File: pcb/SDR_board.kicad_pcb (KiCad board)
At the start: 4 copper layers, 100 x 100 mm, 469 parts, among them J1 USB_B_Mini, J201 Molex 73251-1150 SMA, J301 Molex 73251-1150 SMA, J401 Molex 73251-1150 SMA, J501 Molex 73251-1150 SMA, SW1 SW_Push, U1 AMS1117-3.3, U2 NB3L553, U201 BGA2803, U202 MSi001-Q40, U203 MAX19777AZA+, U204 ADS7883, U205 LMV712-N, U206 MAX19777AZA+, U207 ADS7883, U3 CY7C68013A-56PVX, U301 BGA2803, U302 MSi001-Q40, U303 MAX19777AZA+, U304 ADS7883, U305 LMV712-N, U306 MAX19777AZA+, U307 ADS7883, U401 BGA2803, U402 MSi001-Q40, U403 MAX19777AZA+, U404 ADS7883, U405 LMV712-N, U406 MAX19777AZA+, U407 ADS7883, U5 24LC128, U501 BGA2803, U502 MSi001-Q40, U503 MAX19777AZA+, U504 ADS7883, U505 LMV712-N, U506 MAX19777AZA+, U507 ADS7883, U6 MCP1825S, X1 XO32, X2 XO32

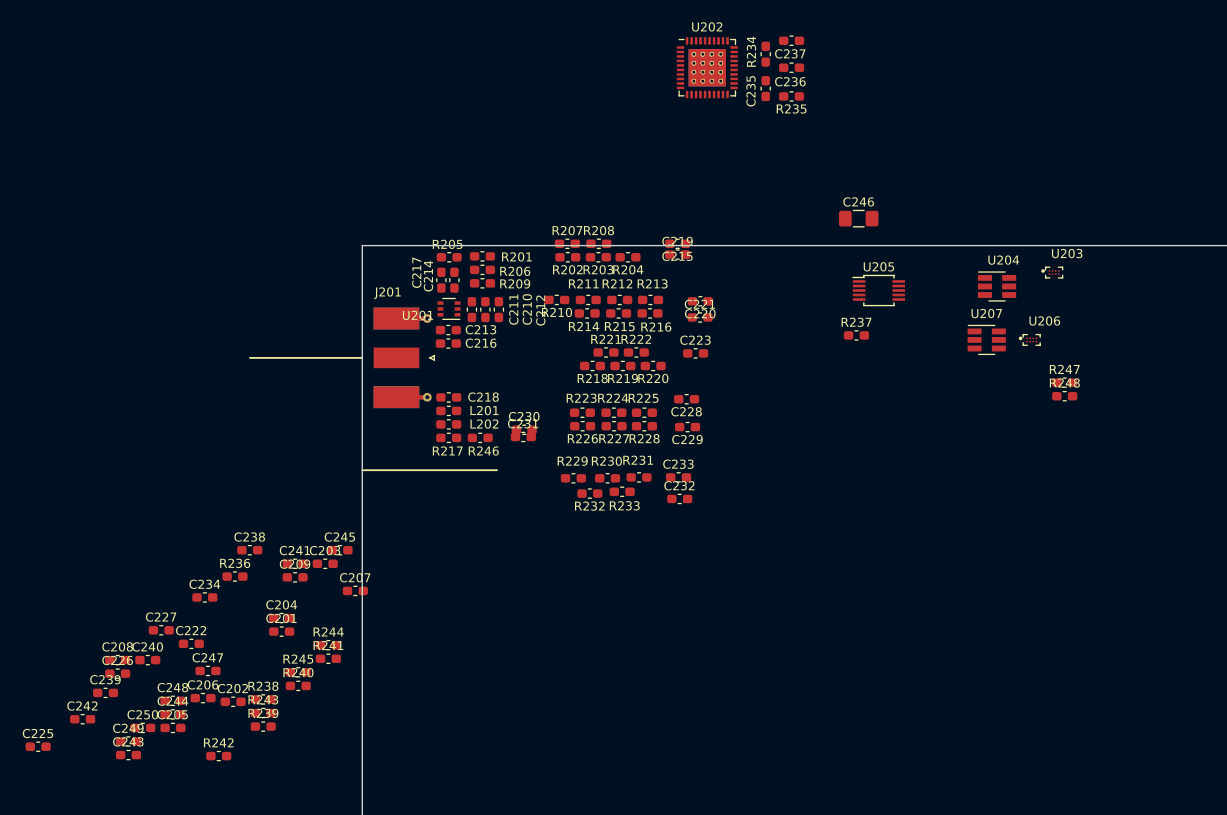
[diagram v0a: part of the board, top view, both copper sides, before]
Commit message: more component layout
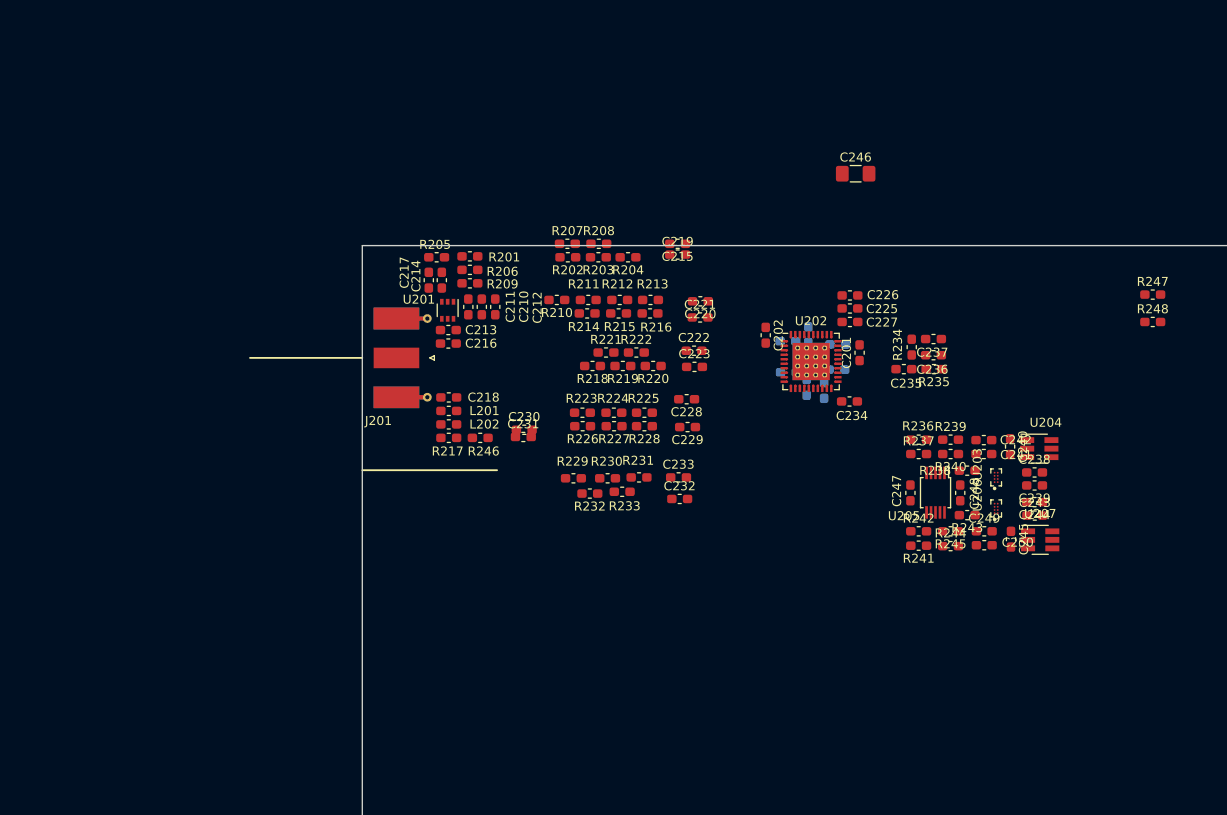
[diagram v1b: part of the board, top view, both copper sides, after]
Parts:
- C203, C204, C205, C206, C207, C208, C209: moved to B.Cu
- moved C239 105.9 mm to (99.8, 46.7), turned to 180 degrees
- moved C242 105.0 mm to (94.2, 41.6)
- moved C243 104.3 mm to (99.8, 50.0)
- moved C225 102.7 mm to (79.3, 27.0), turned to 180 degrees
- moved C240 98.9 mm to (97.1, 42.4), turned to 270 degrees
- moved C244 98.8 mm to (99.8, 48.5), turned to 180 degrees
- moved C249 98.1 mm to (94.2, 51.8)
- moved C250 95.8 mm to (94.2, 53.4)
- moved C226 91.7 mm to (79.3, 25.6), turned to 180 degrees
- moved C248 90.6 mm to (91.5, 47.5), turned to 90 degrees
- moved C238 87.8 mm to (99.8, 45.2)
- moved C208 87.5 mm to (77.9, 31.0), turned to 180 degrees
- moved C227 84.0 mm to (79.3, 28.5)
- moved R239 82.9 mm to (90.5, 41.6)
- moved R238 82.4 mm to (92.3, 45.0), turned to 180 degrees
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
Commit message: Got a channel fully laid out. Setup trace profiles
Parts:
- C201, C202, C210, C211, C212, C219, C221, C225, C226: moved to B.Cu
- U202, U302, U402, U502: footprint Package_DFN_QFN:Texas_S-PVQFN-N40_EP4.15x4.15mm_ThermalVias -> Package_DFN_QFN:Texas_S-PVQFN-N40_EP4.15x4.15mm
- moved C523 175.7 mm to (76.8, 71.4), turned to 90 degrees
- moved C532 172.6 mm to (78.3, 73.0), turned to 90 degrees
- moved R535 171.7 mm to (76.8, 74.7), turned to 90 degrees
- moved C530 171.5 mm to (79.8, 73.0), turned to 90 degrees
- moved R511 170.4 mm to (81.3, 73.0), turned to 90 degrees
- moved R543 168.6 mm to (78.3, 76.4), turned to 90 degrees
- moved R521 167.8 mm to (76.8, 78.1), turned to 90 degrees
- moved C515 167.5 mm to (82.8, 74.5), turned to 90 degrees
- moved R545 167.5 mm to (79.8, 76.4), turned to 90 degrees
- moved C540 166.4 mm to (84.3, 74.5), turned to 90 degrees
- moved C534 166.3 mm to (81.3, 76.4), turned to 90 degrees
- moved C547 165.3 mm to (85.8, 74.5), turned to 90 degrees
- moved R525 164.7 mm to (78.3, 79.7), turned to 90 degrees
- moved C518 163.9 mm to (76.8, 81.4), turned to 90 degrees
- moved R529 163.5 mm to (79.8, 79.7), turned to 90 degrees
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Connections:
- C241 pad 1: /Channel 1/BUFFERED_SINGLE_I -> /Channel 1/BUFFERED_SINGLE_Q
- C242 pad 1: /Channel 1/BUFFERED_SINGLE_I -> /Channel 1/BUFFERED_SINGLE_Q
- C249 pad 1: /Channel 1/BUFFERED_SINGLE_Q -> /Channel 1/BUFFERED_SINGLE_I
- C250 pad 1: /Channel 1/BUFFERED_SINGLE_Q -> /Channel 1/BUFFERED_SINGLE_I
- C341 pad 1: /Channel 2/BUFFERED_SINGLE_I -> /Channel 2/BUFFERED_SINGLE_Q
- C342 pad 1: /Channel 2/BUFFERED_SINGLE_I -> /Channel 2/BUFFERED_SINGLE_Q
- C349 pad 1: /Channel 2/BUFFERED_SINGLE_Q -> /Channel 2/BUFFERED_SINGLE_I
- C350 pad 1: /Channel 2/BUFFERED_SINGLE_Q -> /Channel 2/BUFFERED_SINGLE_I
- C441 pad 1: /Channel 3/BUFFERED_SINGLE_I -> /Channel 3/BUFFERED_SINGLE_Q
- C442 pad 1: /Channel 3/BUFFERED_SINGLE_I -> /Channel 3/BUFFERED_SINGLE_Q
- C449 pad 1: /Channel 3/BUFFERED_SINGLE_Q -> /Channel 3/BUFFERED_SINGLE_I
- C450 pad 1: /Channel 3/BUFFERED_SINGLE_Q -> /Channel 3/BUFFERED_SINGLE_I
- C541 pad 1: /Channel 4/BUFFERED_SINGLE_I -> /Channel 4/BUFFERED_SINGLE_Q
- C542 pad 1: /Channel 4/BUFFERED_SINGLE_I -> /Channel 4/BUFFERED_SINGLE_Q
- C549 pad 1: /Channel 4/BUFFERED_SINGLE_Q -> /Channel 4/BUFFERED_SINGLE_I
- C550 pad 1: /Channel 4/BUFFERED_SINGLE_Q -> /Channel 4/BUFFERED_SINGLE_I
- R236 pad 2: /Channel 1/I_P -> /Channel 1/Q_P
- R238 pad 1: /Channel 1/BUFFERED_SINGLE_I -> /Channel 1/BUFFERED_SINGLE_Q
- R239 pad 2: /Channel 1/I_N -> /Channel 1/Q_N
- R241 pad 2: /Channel 1/Q_P -> /Channel 1/I_P
- R243 pad 1: /Channel 1/BUFFERED_SINGLE_Q -> /Channel 1/BUFFERED_SINGLE_I
- R244 pad 2: /Channel 1/Q_N -> /Channel 1/I_N
- R336 pad 2: /Channel 2/I_P -> /Channel 2/Q_P
- R338 pad 1: /Channel 2/BUFFERED_SINGLE_I -> /Channel 2/BUFFERED_SINGLE_Q
- R339 pad 2: /Channel 2/I_N -> /Channel 2/Q_N
- R341 pad 2: /Channel 2/Q_P -> /Channel 2/I_P
- R343 pad 1: /Channel 2/BUFFERED_SINGLE_Q -> /Channel 2/BUFFERED_SINGLE_I
- R344 pad 2: /Channel 2/Q_N -> /Channel 2/I_N
- R436 pad 2: /Channel 3/I_P -> /Channel 3/Q_P
- R438 pad 1: /Channel 3/BUFFERED_SINGLE_I -> /Channel 3/BUFFERED_SINGLE_Q
- R439 pad 2: /Channel 3/I_N -> /Channel 3/Q_N
- R441 pad 2: /Channel 3/Q_P -> /Channel 3/I_P
- R443 pad 1: /Channel 3/BUFFERED_SINGLE_Q -> /Channel 3/BUFFERED_SINGLE_I
- R444 pad 2: /Channel 3/Q_N -> /Channel 3/I_N
- R536 pad 2: /Channel 4/I_P -> /Channel 4/Q_P
- R538 pad 1: /Channel 4/BUFFERED_SINGLE_I -> /Channel 4/BUFFERED_SINGLE_Q
- R539 pad 2: /Channel 4/I_N -> /Channel 4/Q_N
- R541 pad 2: /Channel 4/Q_P -> /Channel 4/I_P
- R543 pad 1: /Channel 4/BUFFERED_SINGLE_Q -> /Channel 4/BUFFERED_SINGLE_I
- R544 pad 2: /Channel 4/Q_N -> /Channel 4/I_N
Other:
- net class 50_ohm_single added: clearance 0.3, trace_width 0.1468, via_dia 0.8, via_drill 0.45
- net class 90 Ohm diff added: clearance 0.2, trace_width 0.25, via_dia 0.8, via_drill 0.45
- net class Default: trace_width 0.25 -> 0.1468; via_drill 0.4 -> 0.45
- net class Power added: clearance 0.2, trace_width 0.5, via_dia 0.8, via_drill 0.45
- net class other general added: clearance 0.2, trace_width 0.2, via_dia 0.8, via_drill 0.45
- rule trace_min: 0.2 -> 0.127
- rule via_min_drill: 0.3 -> 0.2

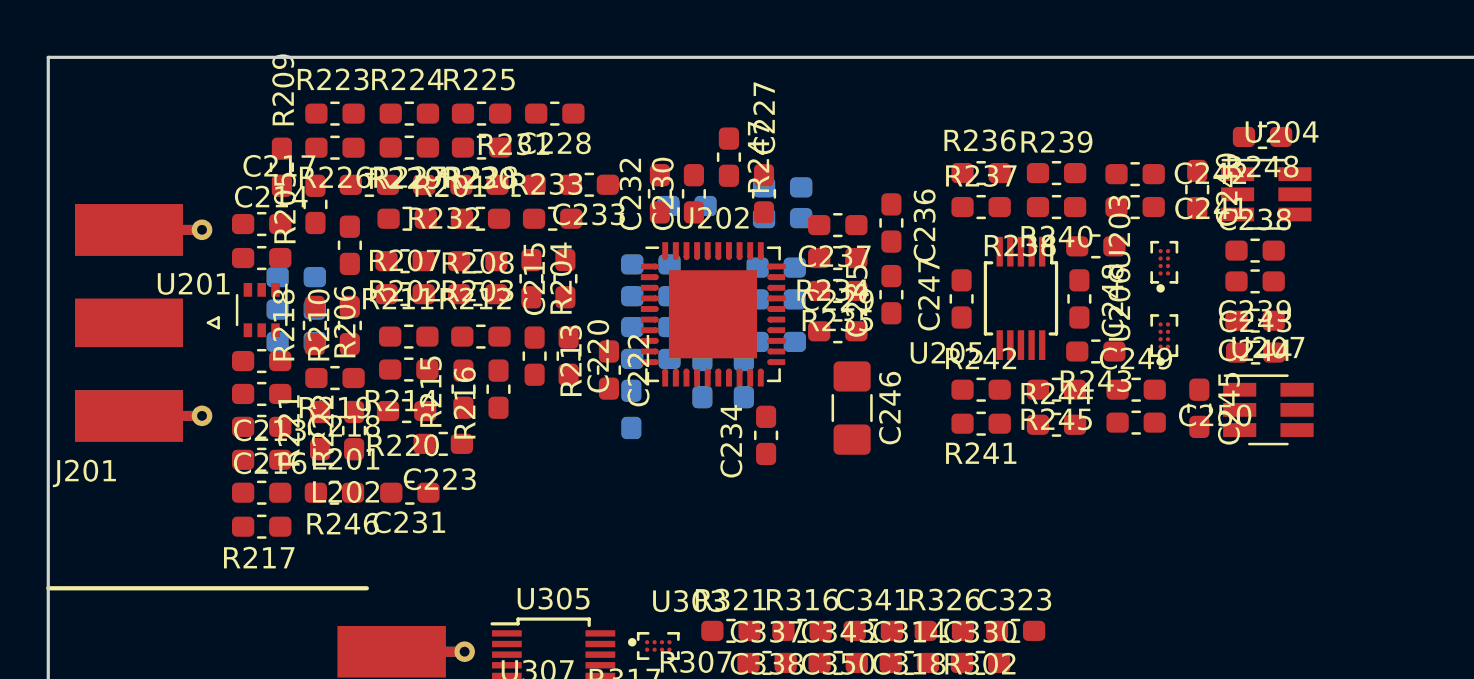
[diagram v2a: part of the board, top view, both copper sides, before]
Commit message: Tuner module mostly wired up, just gotta duplicate them and connect them together
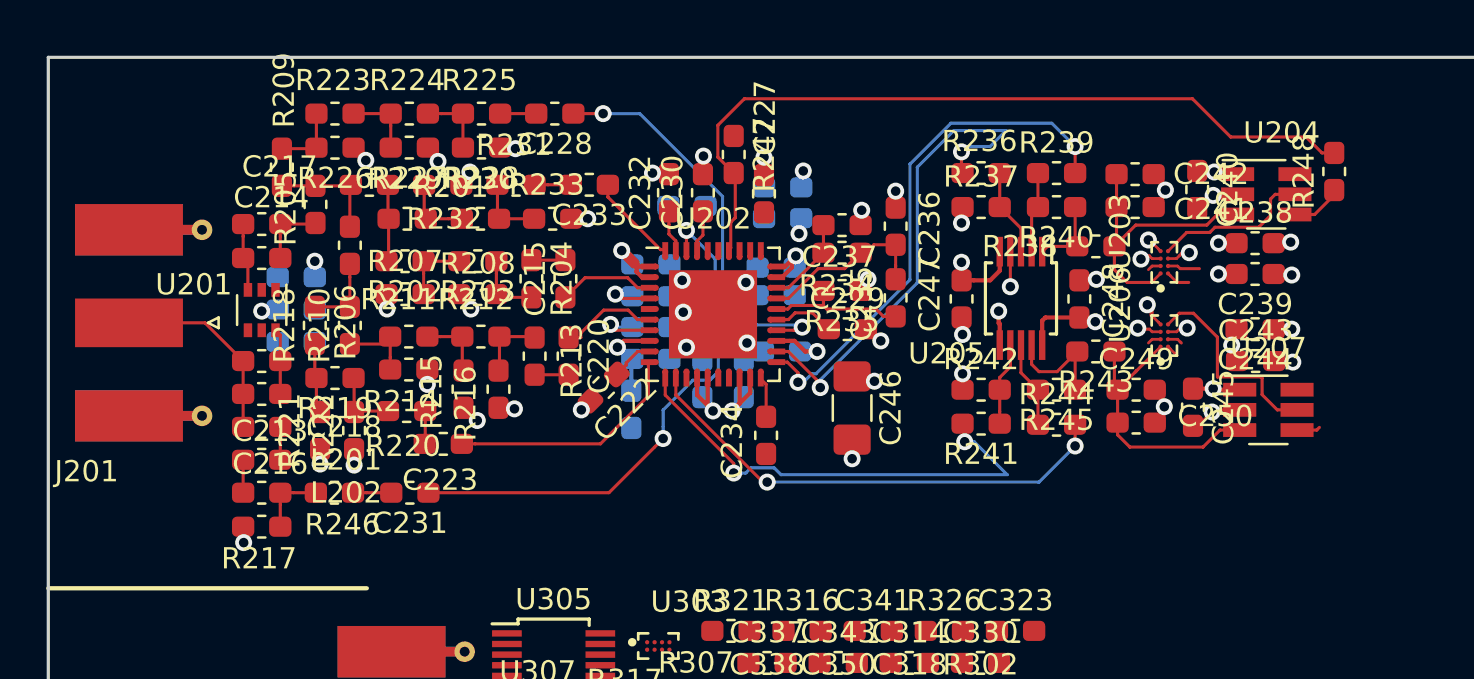
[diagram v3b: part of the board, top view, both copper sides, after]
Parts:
- moved R248 3.75 mm to (85.5, 25.4), turned to 90 degrees
- moved C222 0.86 mm to (51.1, 35.5), turned to 225 degrees
- moved C207 0.51 mm to (59.5, 33.9)
- moved C229 0.46 mm to (62.6, 32.8)
- moved C230 0.43 mm to (55.8, 26.4)
- moved C232 0.43 mm to (54.2, 26.4)
- moved C243 0.40 mm to (81.8, 34.3)
- moved C244 0.40 mm to (81.8, 32.8)
- moved C238 0.35 mm to (81.8, 28.8)
- moved C239 0.35 mm to (81.8, 30.2)
- moved R234 0.32 mm to (62.4, 29.2)
- moved C245 0.30 mm to (78.9, 36.5)
- moved R247 0.26 mm to (57.3, 24.6)
- moved C235 0.25 mm to (64.9, 31.3)
- moved C236 0.25 mm to (64.9, 27.9)
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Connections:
- U203 pad A1: /Channel 1/BUFFERED_SINGLE_I -> /Channel 1/BUFFERED_SINGLE_Q
- U203 pad B4: /Channel 1/I_DOUT -> /Channel 1/Q_DOUT
- U204 pad 3: /Channel 1/BUFFERED_SINGLE_I -> /Channel 1/BUFFERED_SINGLE_Q
- U204 pad 5: /Channel 1/I_DOUT -> /Channel 1/Q_DOUT
- U206 pad A1: /Channel 1/BUFFERED_SINGLE_Q -> /Channel 1/BUFFERED_SINGLE_I
- U206 pad B4: /Channel 1/Q_DOUT -> /Channel 1/I_DOUT
- U207 pad 3: /Channel 1/BUFFERED_SINGLE_Q -> /Channel 1/BUFFERED_SINGLE_I
- U207 pad 5: /Channel 1/Q_DOUT -> /Channel 1/I_DOUT
- U303 pad A1: /Channel 2/BUFFERED_SINGLE_I -> /Channel 2/BUFFERED_SINGLE_Q
- U303 pad B4: /Channel 2/I_DOUT -> /Channel 2/Q_DOUT
- U304 pad 3: /Channel 2/BUFFERED_SINGLE_I -> /Channel 2/BUFFERED_SINGLE_Q
- U304 pad 5: /Channel 2/I_DOUT -> /Channel 2/Q_DOUT
- U306 pad A1: /Channel 2/BUFFERED_SINGLE_Q -> /Channel 2/BUFFERED_SINGLE_I
- U306 pad B4: /Channel 2/Q_DOUT -> /Channel 2/I_DOUT
- U307 pad 3: /Channel 2/BUFFERED_SINGLE_Q -> /Channel 2/BUFFERED_SINGLE_I
- U307 pad 5: /Channel 2/Q_DOUT -> /Channel 2/I_DOUT
- U403 pad A1: /Channel 3/BUFFERED_SINGLE_I -> /Channel 3/BUFFERED_SINGLE_Q
- U403 pad B4: /Channel 3/I_DOUT -> /Channel 3/Q_DOUT
- U404 pad 3: /Channel 3/BUFFERED_SINGLE_I -> /Channel 3/BUFFERED_SINGLE_Q
- U404 pad 5: /Channel 3/I_DOUT -> /Channel 3/Q_DOUT
- U406 pad A1: /Channel 3/BUFFERED_SINGLE_Q -> /Channel 3/BUFFERED_SINGLE_I
- U406 pad B4: /Channel 3/Q_DOUT -> /Channel 3/I_DOUT
- U407 pad 3: /Channel 3/BUFFERED_SINGLE_Q -> /Channel 3/BUFFERED_SINGLE_I
- U407 pad 5: /Channel 3/Q_DOUT -> /Channel 3/I_DOUT
- U503 pad A1: /Channel 4/BUFFERED_SINGLE_I -> /Channel 4/BUFFERED_SINGLE_Q
- U503 pad B4: /Channel 4/I_DOUT -> /Channel 4/Q_DOUT
- U504 pad 3: /Channel 4/BUFFERED_SINGLE_I -> /Channel 4/BUFFERED_SINGLE_Q
- U504 pad 5: /Channel 4/I_DOUT -> /Channel 4/Q_DOUT
- U506 pad A1: /Channel 4/BUFFERED_SINGLE_Q -> /Channel 4/BUFFERED_SINGLE_I
- U506 pad B4: /Channel 4/Q_DOUT -> /Channel 4/I_DOUT
- U507 pad 3: /Channel 4/BUFFERED_SINGLE_Q -> /Channel 4/BUFFERED_SINGLE_I
- U507 pad 5: /Channel 4/Q_DOUT -> /Channel 4/I_DOUT
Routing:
- net Net-(R247-Pad2): track 0.00 -> 36.9 mm
- net +3.3VA: track 0.00 -> 32.1 mm, vias 0 -> 18
- net Net-(C231-Pad1): track 0.00 -> 25.0 mm, vias 0 -> 2
- net /Channel 1/Q_N: track 0.00 -> 24.6 mm, vias 0 -> 2
- net /Channel 1/Q_P: track 0.00 -> 23.5 mm, vias 0 -> 2
- net /Channel 1/I_N: track 0.00 -> 23.0 mm, vias 0 -> 2
- net /Channel 1/I_P: track 0.00 -> 22.4 mm, vias 0 -> 2
- net Net-(C228-Pad1): track 0.00 -> 18.3 mm, vias 0 -> 2
- net /Channel 1/BUFFERED_SINGLE_Q: track 0.00 -> 13.6 mm
- net /Channel 1/BUFFERED_SINGLE_I: track 0.00 -> 13.3 mm
- net GND: track 0.00 -> 12.7 mm, vias 0 -> 47
- net Net-(C223-Pad1): track 0.00 -> 11.3 mm
- net /Channel 1/I_DOUT: track 0.00 -> 9.73 mm
- net Net-(C213-Pad2): track 0.00 -> 9.22 mm
- net Net-(C235-Pad1): track 0.00 -> 8.33 mm
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- added copper zone on Inner_3_PWR.Cu, net +3.3VA
- added copper zone on Inner_3_PWR.Cu, net +3V3
- added copper zone on Inner_2_GND.Cu, net GND
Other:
- net class 50_ohm_single: clearance 0.3 -> 0.2
- net class Power: trace_width 0.5 -> 0.2

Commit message: few more routing changes
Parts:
- moved C209 0.64 mm to (54.6, 26.6)
- moved C230 0.64 mm to (55.3, 26.0)
- moved C232 0.64 mm to (53.7, 26.0)
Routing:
- net GND: track 12.7 -> 80.2 mm, vias 47 -> 49
- net +3.3VA: track 32.1 -> 50.5 mm, vias 18 -> 19
- net +3V3: track 0.00 -> 5.22 mm, vias 0 -> 1
- net /Channel 1/Q_P: track 23.5 -> 18.7 mm
- net /Channel 1/Q_N: track 24.6 -> 21.8 mm
- net Net-(R247-Pad2): track 36.9 -> 35.3 mm
- net Net-(C231-Pad1): track 25.0 -> 26.4 mm
- net Net-(C230-Pad1): track 1.92 -> 2.71 mm
- net Net-(C232-Pad1): track 1.94 -> 2.72 mm
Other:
- net class Power: trace_width 0.2 -> 0.3
